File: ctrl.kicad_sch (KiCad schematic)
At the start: 23 parts, among them J5 Conn_01x12-Socket, J6 Conn_01x12-Socket, J7 Conn_01x12-Header, J8 Conn_01x12-Header, M1 Fan_4pin, M2 Fan_4pin, U30 T-Display-S3, U32 EMC2302-1, U33 TXU0102-DCU, U37 TMP1075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

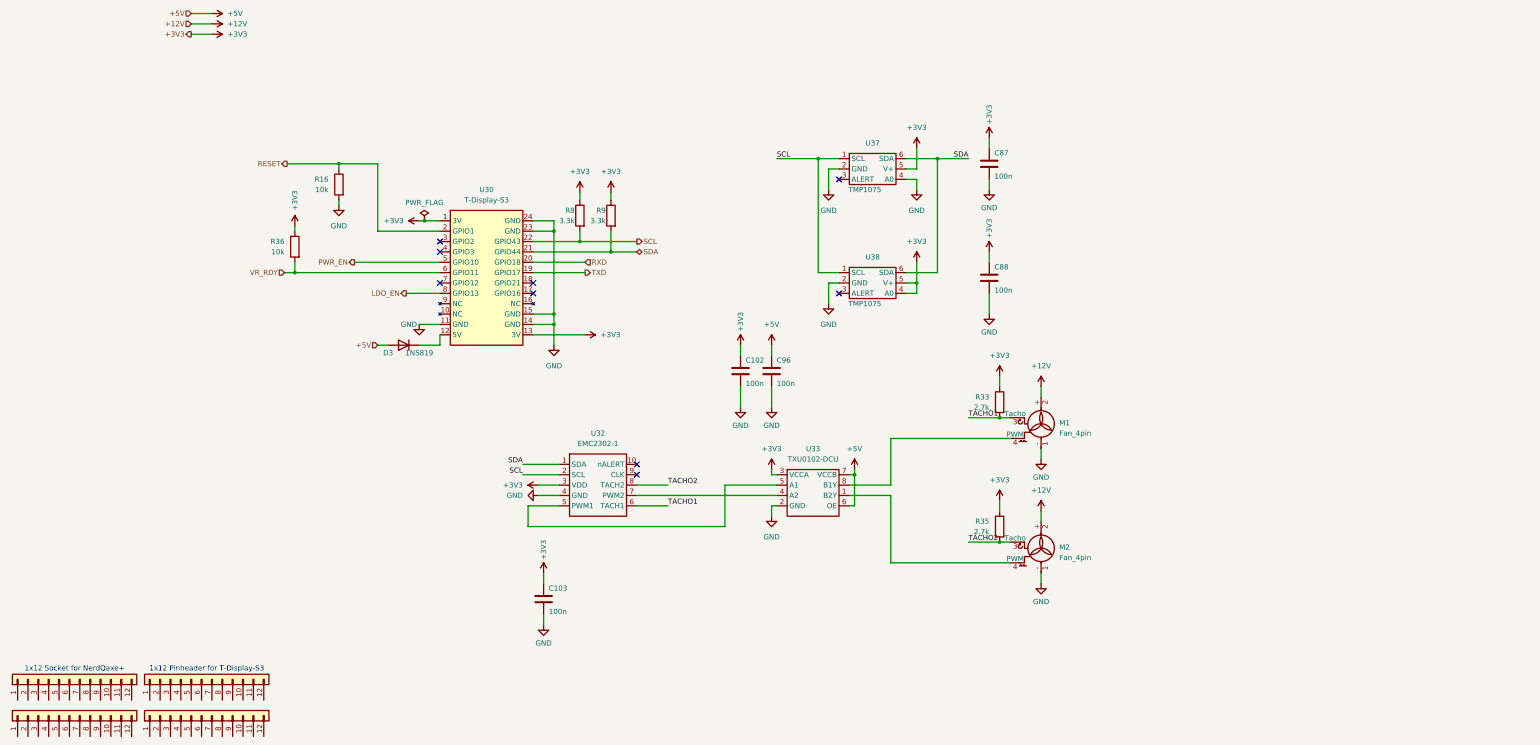
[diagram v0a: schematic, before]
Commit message: power in components to PCB
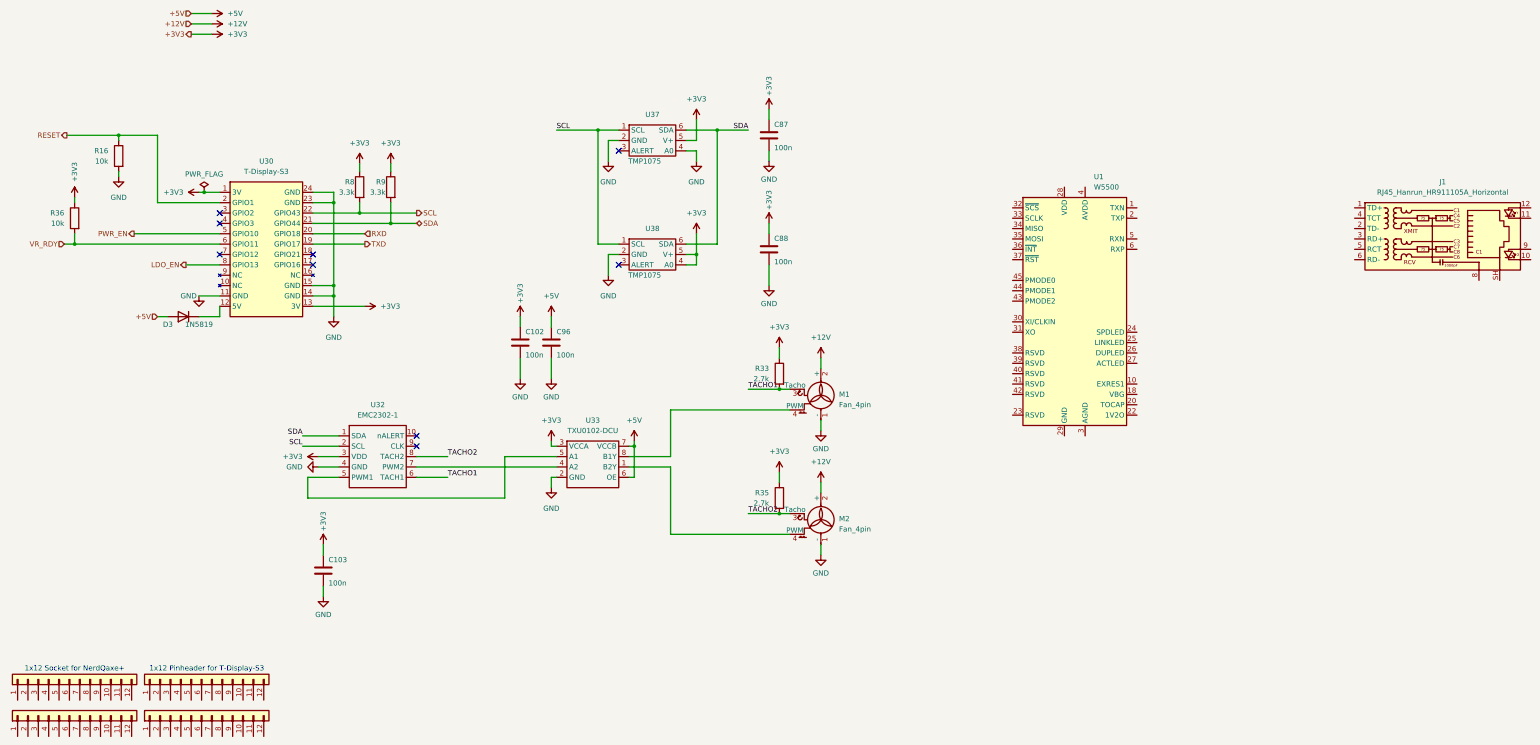
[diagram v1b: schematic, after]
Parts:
- added J1: RJ45_Hanrun_HR911105A_Horizontal, Connector_RJ:RJ45_Hanrun_HR911105A_Horizontal, symbol Connector:RJ45_Hanrun_HR911105A_Horizontal
- added U1: W5500, Package_QFP:LQFP-48_7x7mm_P0.5mm, symbol Interface_Ethernet:W5500
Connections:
- new net: U1.11 (AVDD), U1.15 (AVDD), U1.17 (AVDD), U1.21 (AVDD), U1.4 (AVDD), U1.8 (AVDD)
- new net: U1.14 (AGND), U1.16 (AGND), U1.19 (AGND), U1.3 (AGND), U1.48 (AGND), U1.9 (AGND)
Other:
- moved on the sheet: C102, C103, C87, C88, C96, D3, M1, M2, R16, R33, R35, R36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
